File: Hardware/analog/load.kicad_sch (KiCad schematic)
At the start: 36 parts, among them J201 Würth 74651194R, J202 Würth 74651194R, Q201 IXTH80N075L2, Q202 IXTH80N075L2, U201 ADA4522-2, U202 LM431SC, U203 LMT86LMT, U204 ADA4522-2, U205 LM431SC

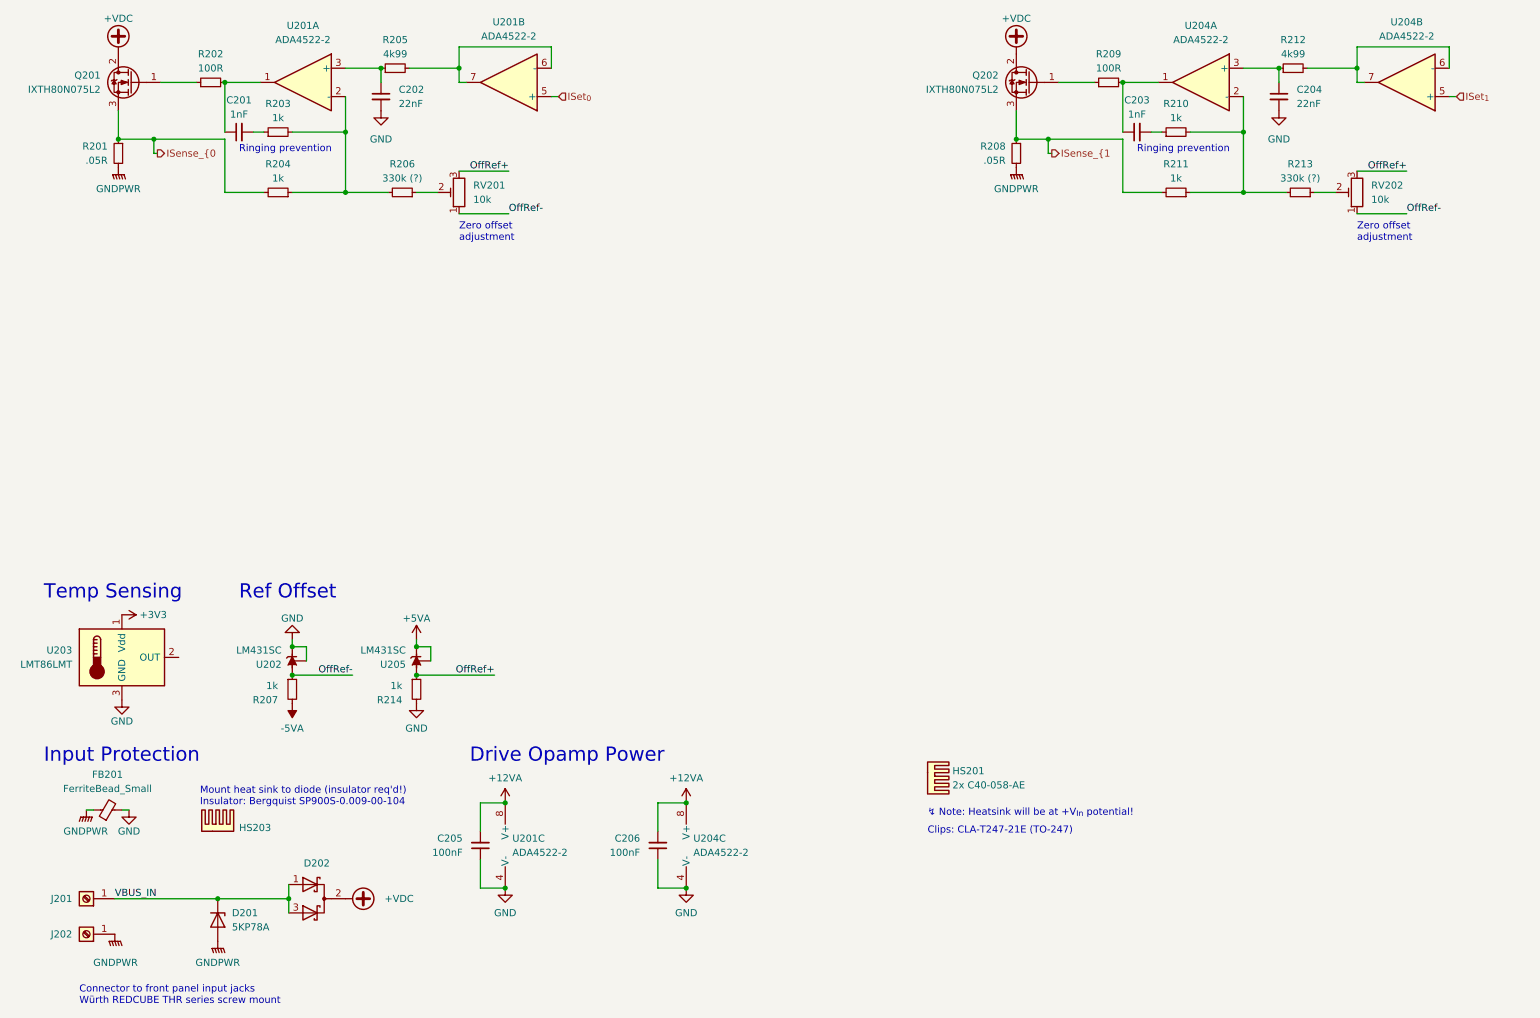
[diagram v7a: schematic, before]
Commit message: Added more decoupling for reference
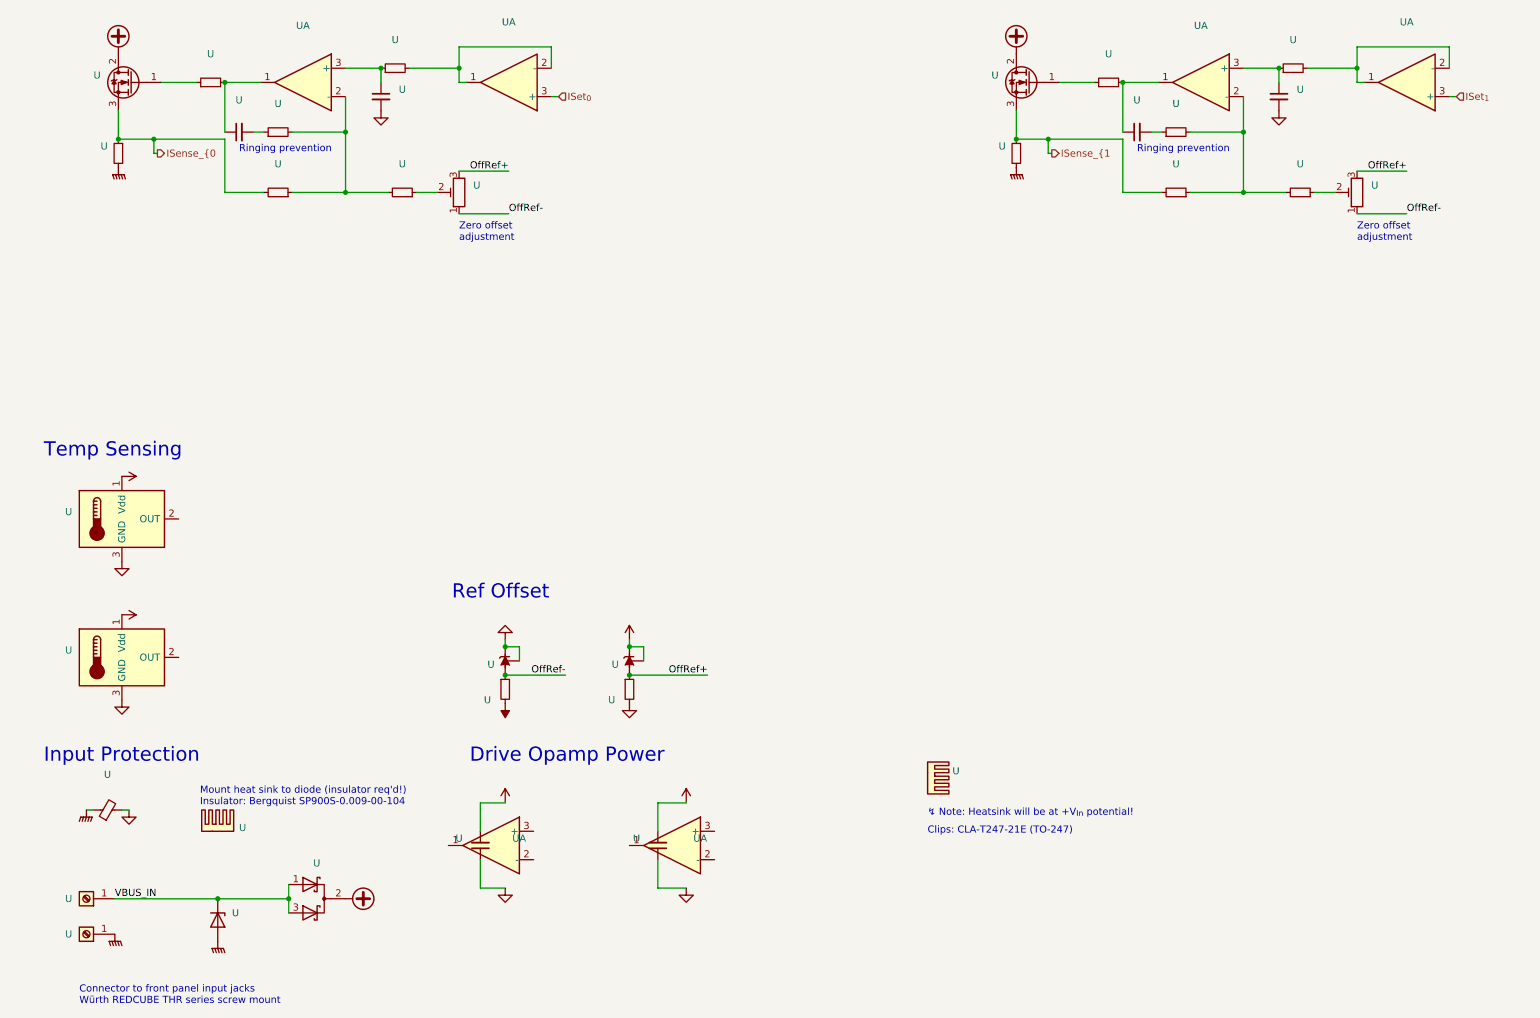
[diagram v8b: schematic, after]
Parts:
- added U: (no value), symbol programmable-load:LMT86LPM
- U: renamed from R203; value 1k -> (none); footprint Resistor_SMD:R_0805_2012Metric_Pad1.20x1.40mm_HandSolder -> (none)
- U: renamed from U204; value ADA4522-2 -> (none); footprint Package_SO:SOIC-8_3.9x4.9mm_P1.27mm -> (none)
- U: renamed from R211; value 1k -> (none); footprint Resistor_SMD:R_0805_2012Metric_Pad1.20x1.40mm_HandSolder -> (none)
- U: renamed from R209; value 100R -> (none); footprint Resistor_SMD:R_0805_2012Metric_Pad1.20x1.40mm_HandSolder -> (none)
- U: renamed from R210; value 1k -> (none); footprint Resistor_SMD:R_0805_2012Metric_Pad1.20x1.40mm_HandSolder -> (none)
- U: renamed from R213; value 330k (?) -> (none); footprint Resistor_SMD:R_0805_2012Metric_Pad1.20x1.40mm_HandSolder -> (none)
- U: renamed from J202; value Würth 74651194R -> (none); footprint programmable-load:WE-74651194 -> (none)
- U: renamed from C202; value 22nF -> (none); footprint Capacitor_SMD:C_0805_2012Metric_Pad1.18x1.45mm_HandSolder -> (none)
- U: renamed from R201; value .05R -> (none); footprint programmable-load:TO-247-2_Vertical -> (none)
- U: renamed from U205; value LM431SC -> (none); footprint Package_TO_SOT_SMD:SOT-23 -> (none)
- U: renamed from C203; value 1nF -> (none); footprint Capacitor_SMD:C_0805_2012Metric_Pad1.18x1.45mm_HandSolder -> (none)
- U: renamed from R205; value 4k99 -> (none); footprint Resistor_SMD:R_0805_2012Metric_Pad1.20x1.40mm_HandSolder -> (none)
- U: renamed from R204; value 1k -> (none); footprint Resistor_SMD:R_0805_2012Metric_Pad1.20x1.40mm_HandSolder -> (none)
- U: renamed from FB201; value FerriteBead_Small -> (none); footprint Inductor_SMD:L_0805_2012Metric_Pad1.05x1.20mm_HandSolder -> (none)
- U: renamed from HS201; value 2x C40-058-AE -> (none); footprint programmable-load:C40-058-AE-DUAL -> (none)
- U: renamed from Q201; value IXTH80N075L2 -> (none); footprint Package_TO_SOT_THT:TO-247-3_Vertical -> (none)
- U: renamed from R212; value 4k99 -> (none); footprint Resistor_SMD:R_0805_2012Metric_Pad1.20x1.40mm_HandSolder -> (none)
- U: renamed from C206; value 100nF -> (none); footprint Capacitor_SMD:C_0805_2012Metric_Pad1.18x1.45mm_HandSolder -> (none)
- U: renamed from C201; value 1nF -> (none); footprint Capacitor_SMD:C_0805_2012Metric_Pad1.18x1.45mm_HandSolder -> (none)
- U: renamed from RV201; value 10k -> (none); footprint programmable-load:Potentiometer_Nidec_Copal_CT94EY -> (none)
- U: renamed from RV202; value 10k -> (none); footprint programmable-load:Potentiometer_Nidec_Copal_CT94EY -> (none)
- U: renamed from R208; value .05R -> (none); footprint programmable-load:TO-247-2_Vertical -> (none)
- U: renamed from J201; value Würth 74651194R -> (none); footprint programmable-load:WE-74651194 -> (none)
- U: renamed from R202; value 100R -> (none); footprint Resistor_SMD:R_0805_2012Metric_Pad1.20x1.40mm_HandSolder -> (none)
- U: renamed from U201; value ADA4522-2 -> (none); footprint Package_SO:SOIC-8_3.9x4.9mm_P1.27mm -> (none)
- U: renamed from Q202; value IXTH80N075L2 -> (none); footprint Package_TO_SOT_THT:TO-247-3_Vertical -> (none)
- U: renamed from C204; value 22nF -> (none); footprint Capacitor_SMD:C_0805_2012Metric_Pad1.18x1.45mm_HandSolder -> (none)
- U: renamed from U202; value LM431SC -> (none); footprint Package_TO_SOT_SMD:SOT-23 -> (none)
- U: renamed from R214; value 1k -> (none); footprint Resistor_SMD:R_0805_2012Metric_Pad1.20x1.40mm_HandSolder -> (none)
- U: renamed from HS203; value WV-T247-101E -> (none); footprint programmable-load:Ohmite-WA-T247-101E-MFG -> (none)
- U: renamed from D202; value DSA120C150QB -> (none); footprint Package_TO_SOT_THT:TO-247-3_Vertical -> (none)
- U: renamed from U203; value LMT86LMT -> (none); footprint Package_TO_SOT_THT:TO-92_Inline_Wide -> (none)
- U: renamed from C205; value 100nF -> (none); footprint Capacitor_SMD:C_0805_2012Metric_Pad1.18x1.45mm_HandSolder -> (none)
- U: renamed from R207; value 1k -> (none); footprint Resistor_SMD:R_0805_2012Metric_Pad1.20x1.40mm_HandSolder -> (none)
- U: renamed from R206; value 330k (?) -> (none); footprint Resistor_SMD:R_0805_2012Metric_Pad1.20x1.40mm_HandSolder -> (none)
- U: renamed from D201; value 5KP78A -> (none); footprint Diode_THT:D_P600_R-6_P20.00mm_Horizontal -> (none)
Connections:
- net +12VA: no longer U.8 (V+), U.8 (V+)
- net +3V3: now also U.1 (Vdd)
- net GND: now also U.3 (GND); no longer U.4 (V-), U.4 (V-)
- net ISet_{0}: now also U.3 (+); no longer U.5 (+)
- net ISet_{1}: now also U.3 (+); no longer U.5 (+)
- new net: U.1, U.2, U.2 (-) (x2)
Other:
- moved on the sheet: U
